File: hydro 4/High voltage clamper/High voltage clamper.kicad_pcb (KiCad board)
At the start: 2 copper layers, 2 parts, among them Q1 IRF740

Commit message: Updated clamp board
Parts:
- added C1: 47uF, Capacitor_THT:CP_Radial_D8.0mm_P2.50mm, F.Cu at (146.3, 100.3)
- added D2: D, Diode_THT:D_DO-15_P12.70mm_Horizontal, F.Cu at (128.6, 77.1)
- added R1: 10k, Resistor_THT:R_Axial_DIN0207_L6.3mm_D2.5mm_P7.62mm_Horizontal, F.Cu at (114.6, 91.7)
- added R2: 100k, Resistor_THT:R_Axial_DIN0207_L6.3mm_D2.5mm_P7.62mm_Horizontal, F.Cu at (129.0, 103.6)
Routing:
- net Net-(D1-K): track 26.6 -> 58.5 mm
- net -VDC: track 28.2 -> 42.1 mm
- net Net-(D2-A): track 0.00 -> 7.51 mm
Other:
- board outline added: 66.9 x 55 mm

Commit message: Updated schematic
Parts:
- removed C1: 47uF, Capacitor_THT:CP_Radial_D8.0mm_P2.50mm
- removed D1: ZMDxx, Diode_SMD:D_MiniMELF
- removed D2: D, Diode_THT:D_DO-15_P12.70mm_Horizontal
- added RV1: 1M, Potentiometer_THT:Potentiometer_ACP_CA14V-15_Vertical_Hole, F.Cu at (114.8, 81.1)
- R1: value 10k -> 4.7M
- R2: value 100k -> 50 200watt; footprint Resistor_THT:R_Axial_DIN0207_L6.3mm_D2.5mm_P7.62mm_Horizontal -> Resistor_THT:R_Box_L26.0mm_W5.0mm_P20.00mm
- moved R2 36.6 mm to (156.1, 78.9)
- moved R1 21.5 mm to (135.2, 85.6), turned to -90 degrees
- moved Q1 6.95 mm to (153.0, 88.0), turned to -90 degrees
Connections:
- Q1 pad 1: Net-(D1-K) -> Net-(Q1-G)
- Q1 pad 2: Net-(LA1--) -> Net-(Q1-D)
- R1 pad 1: +VDC -> Net-(R1-Pad1)
- R1 pad 2: Net-(D2-A) -> +VDC
- R2 pad 1: -VDC -> Net-(Q1-D)
- R2 pad 2: Net-(D1-K) -> +VDC
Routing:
- net Net-(D1-K): track 58.5 -> 0.00 mm
- net Net-(Q1-G): track 0.00 -> 36.6 mm
- net Net-(R1-Pad1): track 0.00 -> 22.3 mm
- net +VDC: track 0.00 -> 17.6 mm, vias 0 -> 1
- net Net-(Q1-D): track 0.00 -> 14.1 mm
- net -VDC: track 42.1 -> 33.2 mm
- net Net-(D2-A): track 7.51 -> 0.00 mm
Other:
- board size 66.9 x 55 mm -> 56.7 x 37.5 mm

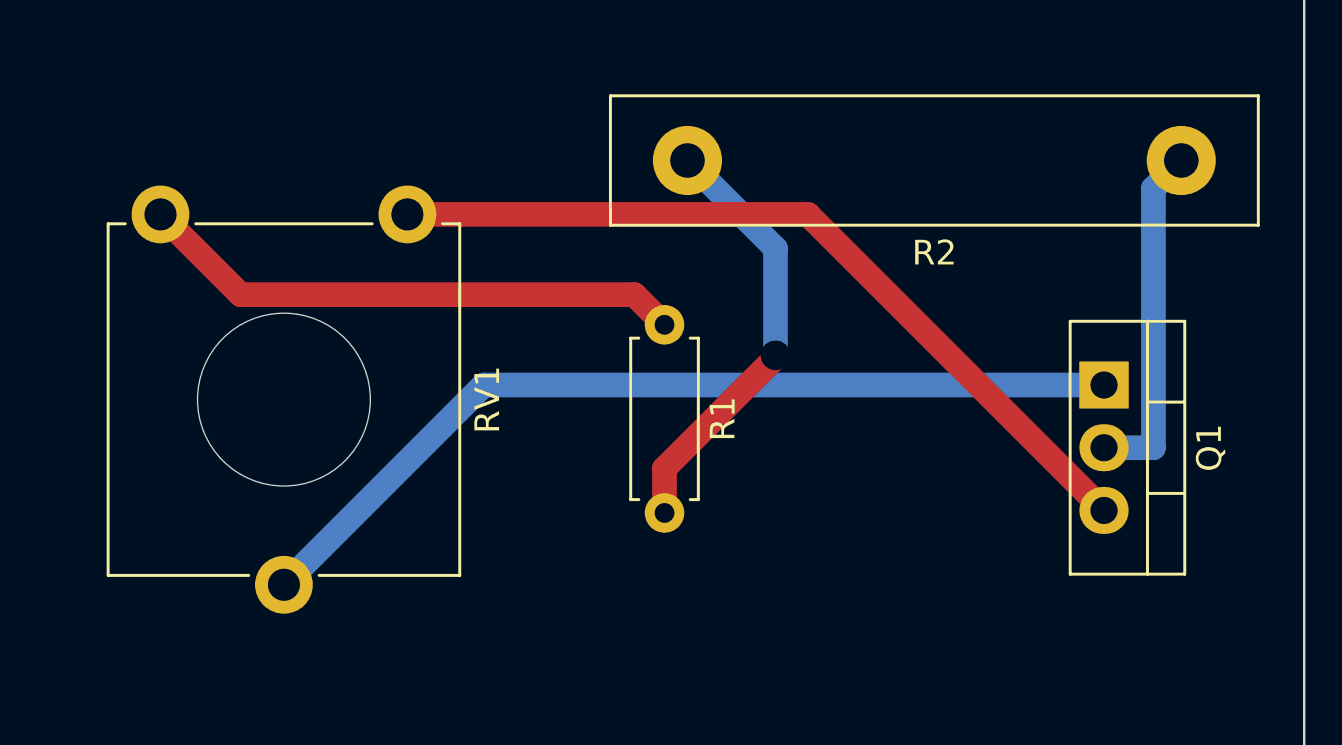
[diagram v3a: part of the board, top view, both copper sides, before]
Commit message: Updated Nozzles
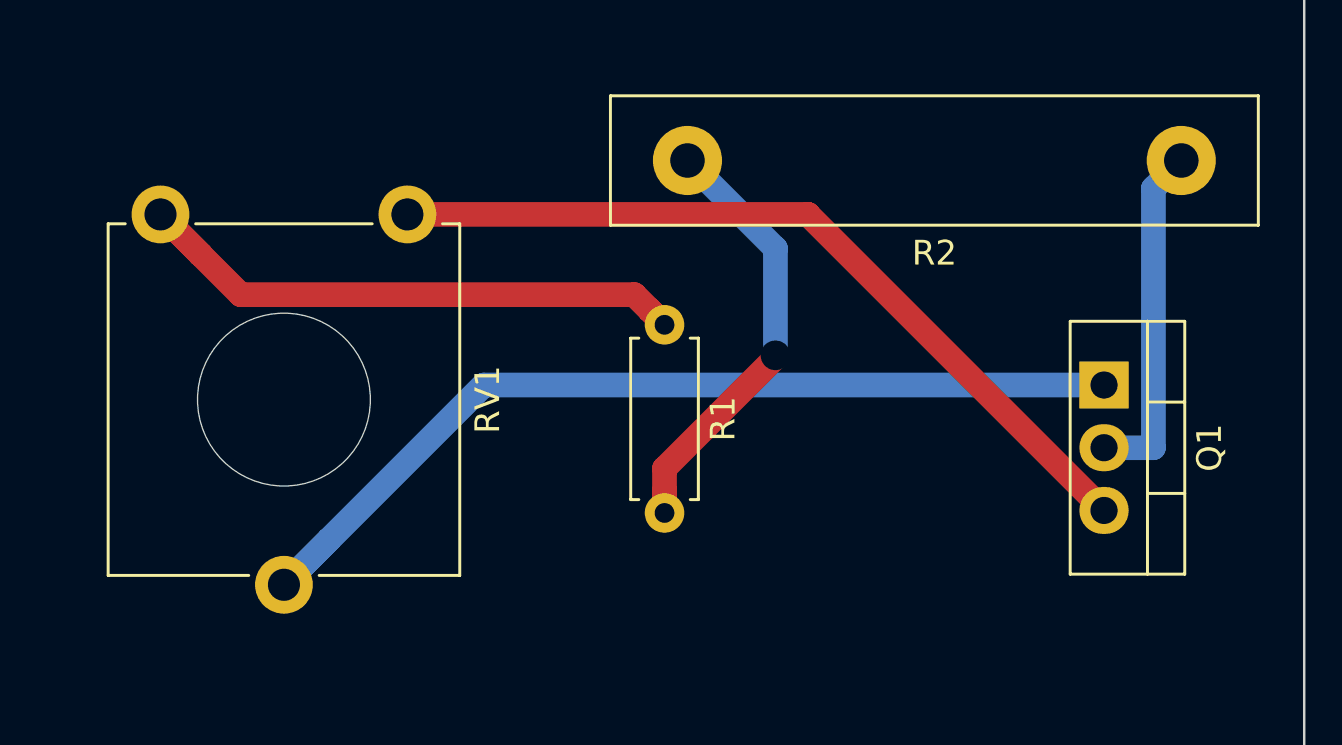
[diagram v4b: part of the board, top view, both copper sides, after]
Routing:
- net Net-(R1-Pad1): track 22.3 -> 25.4 mm
- net Net-(Q1-G): track 36.6 -> 39.1 mm
- net +VDC: track 17.6 -> 18.5 mm
- net Net-(Q1-D): track 14.1 -> 14.9 mm
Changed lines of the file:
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@@
 (kicad_pcb
-	(version 20231212)
+	(version 20240108)
 	(generator "pcbnew")
 	(generator_version "7.99")
@@
 	)
 	(segment
+		(start 124.765 81.1276)
+		(end 124.7648 81.1276)
+		(width 1)
+		(layer "F.Cu")
+		(net 1)
+	)
+	(segment
 		(start 152.979 93.1164)
 		(end 140.9902 81.1276)
@@
 	(segment
 		(start 140.9902 81.1276)
-		(end 124.7648 81.1276)
+		(end 140.99 81.1276)
 		(width 1)
 		(layer "F.Cu")
 		(net 1)
+	)
+	(segment
+		(start 140.99 81.1276)
+		(end 124.765 81.1276)
+		(width 1)
+		(layer "F.Cu")
+		(net 1)
+	)
+	(segment
+		(start 155.5435 79.5079)
+		(end 155.5437 79.5079)
+		(width 1)
+		(layer "B.Cu")
+		(net 2)
+	)
+	(segment
+		(start 155.5437 79.5079)
+		(end 156.1084 78.9432)
+		(width 1)
+		(layer "B.Cu")
+		(net 2)
+	)
+	(segment
+		(start 152.979 90.5764)
+		(end 154.979 90.5764)
+		(width 1)
+		(layer "B.Cu")
+		(net 2)
+	)
+	(segment
+		(start 155.5435 79.5079)
+		(end 156.108 78.9432)
+		(width 1)
+		(layer "B.Cu")
+		(net 2)
 	)
 	(segment
@@
 	)
 	(segment
-		(start 152.979 90.5764)
-		(end 154.979 90.5764)
+		(start 154.979 80.0726)
+		(end 155.5435 79.5079)
 		(width 1)
 		(layer "B.Cu")
@@
 	)
 	(segment
-		(start 154.979 80.0726)
-		(end 156.1084 78.9432)
-		(width 1)
-		(layer "B.Cu")
-		(net 2)
-	)
-	(segment
-		(start 133.9584 84.3776)
-		(end 118.0148 84.3776)
+		(start 118.015 84.3776)
+		(end 116.39 82.7526)
 		(width 1)
 		(layer "F.Cu")
@@
 	)
 	(segment
-		(start 135.1788 85.598)
-		(end 133.9584 84.3776)
+		(start 134.5685 84.9878)
+		(end 134.5686 84.9878)
 		(width 1)
 		(layer "F.Cu")
@@
 	)
 	(segment
-		(start 118.0148 84.3776)
+		(start 135.179 85.598)
+		(end 134.5685 84.9878)
+		(width 1)
+		(layer "F.Cu")
+		(net 3)
+	)
+	(segment
+		(start 116.39 82.7526)
+		(end 114.765 81.1276)
+		(width 1)
+		(layer "F.Cu")
+		(net 3)
+	)
+	(segment
+		(start 134.5686 84.9878)
+		(end 135.1788 85.598)
+		(width 1)
+		(layer "F.Cu")
+		(net 3)
+	)
+	(segment
+		(start 133.958 84.3776)
+		(end 118.015 84.3776)
+		(width 1)
+		(layer "F.Cu")
+		(net 3)
+	)
+	(segment
+		(start 116.3898 82.7526)
 		(end 114.7648 81.1276)
 		(width 1)
@@
 	)
 	(segment
-		(start 139.6723 86.9245)
-		(end 135.1788 91.418)
+		(start 134.5685 84.9878)
+		(end 133.958 84.3776)
+		(width 1)
+		(layer "F.Cu")
+		(net 3)
+	)
+	(segment
+		(start 116.39 82.7526)
+		(end 116.3898 82.7526)
+		(width 1)
+		(layer "F.Cu")
+		(net 3)
+	)
+	(segment
+		(start 135.1788 92.3182)
+		(end 135.1788 93.218)
 		(width 1)
 		(layer "F.Cu")
@@
 	)
 	(segment
-		(start 135.1788 93.218)
-		(end 135.1788 91.418)
+		(start 139.672 86.8347)
+		(end 139.672 86.9245)
 		(width 1)
 		(layer "F.Cu")
@@
 	)
 	(segment
-		(start 139.6723 86.8347)
-		(end 139.6723 86.9245)
+		(start 139.672 86.9245)
+		(end 135.179 91.418)
 		(width 1)
 		(layer "F.Cu")
 		(net 4)
 	)
+	(segment
+		(start 135.179 92.318)
+		(end 135.1788 92.3182)
+		(width 1)
+		(layer "F.Cu")
+		(net 4)
+	)
+	(segment
+		(start 135.179 91.418)
+		(end 135.179 92.318)
+		(width 1)
+		(layer "F.Cu")
+		(net 4)
+	)
+	(segment
+		(start 135.179 92.318)
+		(end 135.179 93.218)
+		(width 1)
+		(layer "F.Cu")
+		(net 4)
+	)
 	(via
-		(at 139.6723 86.8347)
+		(at 139.672 86.8347)
 		(size 1)
 		(drill 1.2)
@@
 	)
 	(segment
-		(start 139.6723 82.5071)
-		(end 139.6723 86.8347)
+		(start 136.108 78.9432)
+		(end 136.1082 78.9434)
 		(width 1)
 		(layer "B.Cu")
@@
 	(segment
 		(start 136.1084 78.9432)
-		(end 139.6723 82.5071)
+		(end 136.1082 78.9434)
 		(width 1)
 		(layer "B.Cu")
@@
 	)
 	(segment
-		(start 127.856 88.0364)
-		(end 119.7648 96.1276)
+		(start 139.672 82.5071)
+		(end 139.672 86.8347)
+		(width 1)
+		(layer "B.Cu")
+		(net 4)
+	)
+	(segment
+		(start 136.1082 78.9434)
+		(end 139.672 82.5071)
+		(width 1)
+		(layer "B.Cu")
+		(net 4)
+	)
+	(segment
+		(start 121.59 94.3026)
+		(end 119.765 96.1276)
 		(width 1)
 		(layer "B.Cu")
@@
 		(width 1)
 		(layer "B.Cu")
+		(net 5)
+	)
+	(segment
+		(start 121.5898 94.3026)
+		(end 119.7648 96.1276)
+		(width 1)
+		(layer "B.Cu")
+		(net 5)
+	)
+	(segment
+		(start 121.59 94.3026)
+		(end 121.5898 94.3026)
+		(width 1)
+		(layer "B.Cu")
+		(net 5)
+	)
+	(segment
+		(start 127.856 88.0364)
+		(end 121.59 94.3026)
+		(width 1)
+		(layer "B.Cu")
